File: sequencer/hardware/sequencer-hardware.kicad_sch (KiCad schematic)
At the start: 47 parts, among them J1 Barrel Jack, J2 40Pin 0.1", J3 USB_B_Micro, J4 Conn_01x02_Male, J5 Conn_01x04, J6 TS Out, SW1 PWR, SW2 SW_Push, U1 L7805_A, U2 L7805_D, U3 ICL7660, U4 NCP1117-3.3_TO252, U5 Opamp_Dual

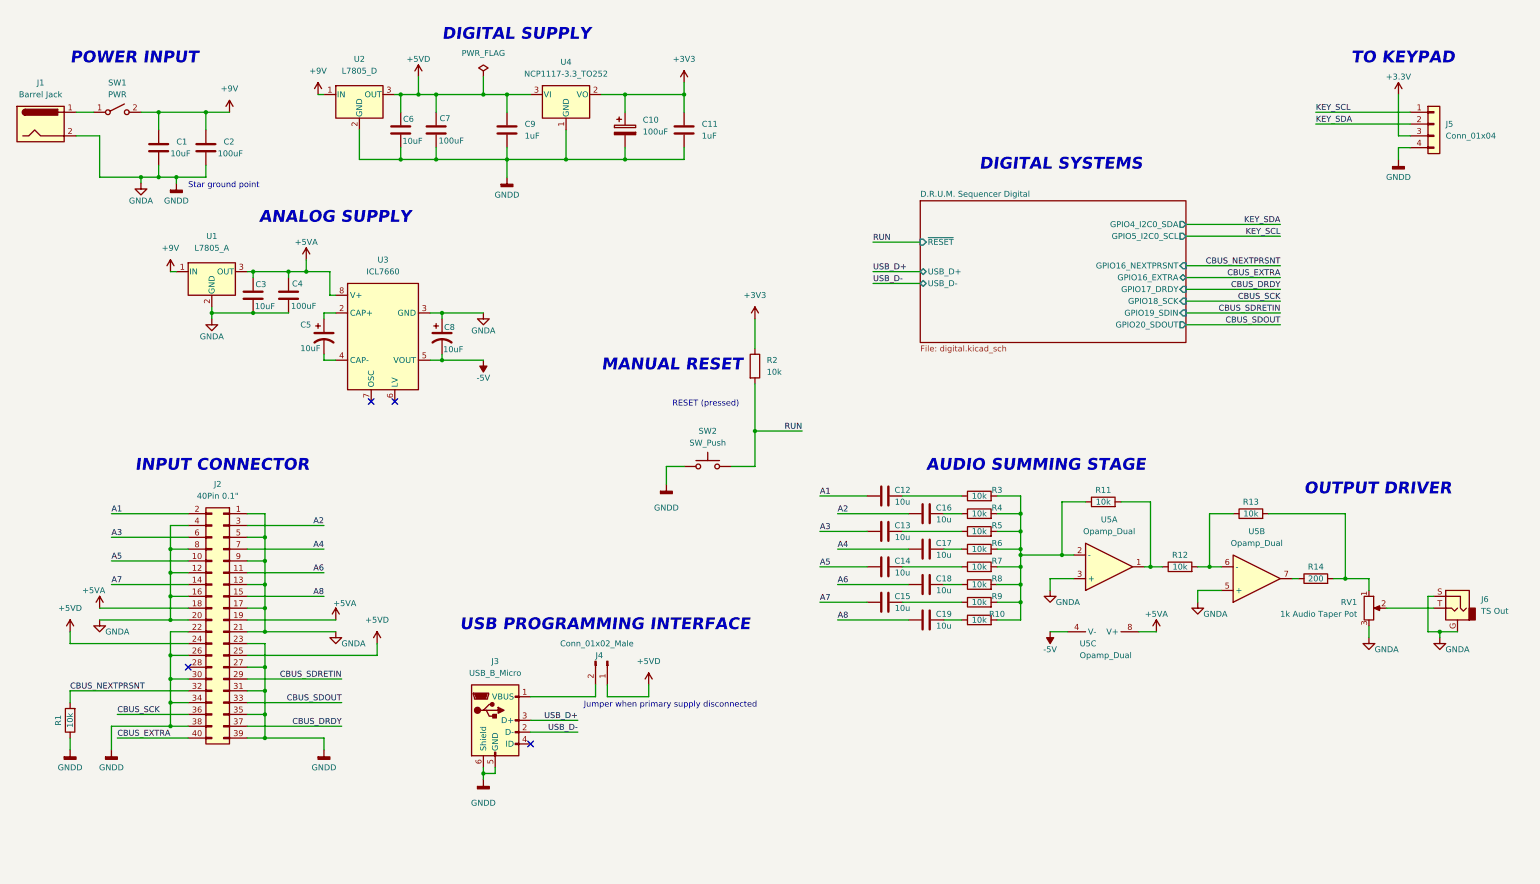
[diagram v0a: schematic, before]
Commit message: Disconnect GNDD from GNDA to prevent routing confusion
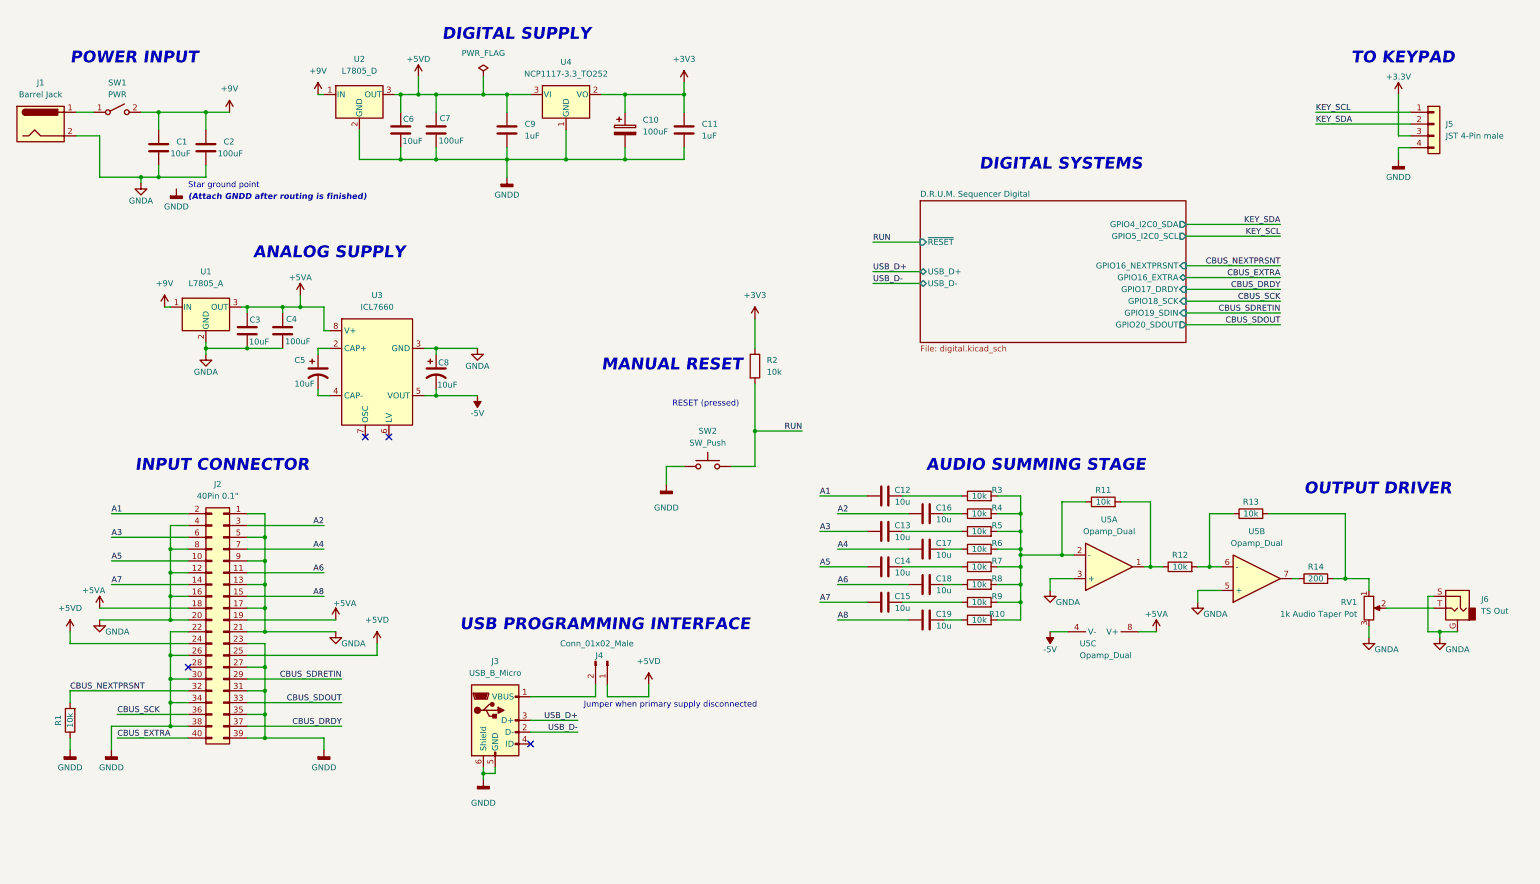
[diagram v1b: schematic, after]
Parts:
- J5: value Conn_01x04 -> JST 4-Pin male; footprint (none) -> Connector_JST:JST_PH_B4B-PH-K_1x04_P2.00mm_Vertical
- R1, R10, R11, R12, R13, R3, R4, R5, R6, R7, R8, R9: footprint (none) -> Resistor_SMD:R_0603_1608Metric_Pad0.98x0.95mm_HandSolder
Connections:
- net GNDA: no longer C10.2, C11.2, C6.2, C7.2, C9.2, J2.22 (Pin_22), J2.23 (Pin_23), J2.26 (Pin_26), J2.27 (Pin_27), J2.30 (Pin_30), J2.31 (Pin_31), J2.34 (Pin_34), J2.35 (Pin_35), J2.38 (Pin_38), J2.39 (Pin_39), J3.5 (GND), J3.6 (Shield), J5.4 (Pin_4), R1.1, SW2.1, U2.2 (GND), U4.1 (GND)
- new net GNDD: C10.2, C11.2, C6.2, C7.2, C9.2, J2.22 (Pin_22), J2.23 (Pin_23), J2.26 (Pin_26), J2.27 (Pin_27), J2.30 (Pin_30), J2.31 (Pin_31), J2.34 (Pin_34), J2.35 (Pin_35), J2.38 (Pin_38), J2.39 (Pin_39), J3.5 (GND), J3.6 (Shield), J5.4 (Pin_4), R1.1, SW2.1, U2.2 (GND), U4.1 (GND)
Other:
- note added: "(Attach GNDD after routing is finished)"
- moved on the sheet: C3, C4, C5, C8, U1, U3

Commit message: Do a lot of random stuff
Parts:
- removed U5: Opamp_Dual, symbol Device:Opamp_Dual
- added U5, U6: OPA703UA, Package_SO:SOIC-8_3.9x4.9mm_P1.27mm, symbol pspice:OPAMP
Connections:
- net +5VA: now also U5.4 (V-), U6.4 (V-)
- net -5V: now also U5.7 (V+), U6.7 (V+)
- net GNDA: now also U5.3 (+), U6.3 (+)
- net at R14.1: now also U6.6
- net at R10.2, R11.1, R3.2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: now also U5.2 (-)
- net at R11.2, R12.1: now also U5.6
- net at R12.2, R13.1: now also U6.2 (-)

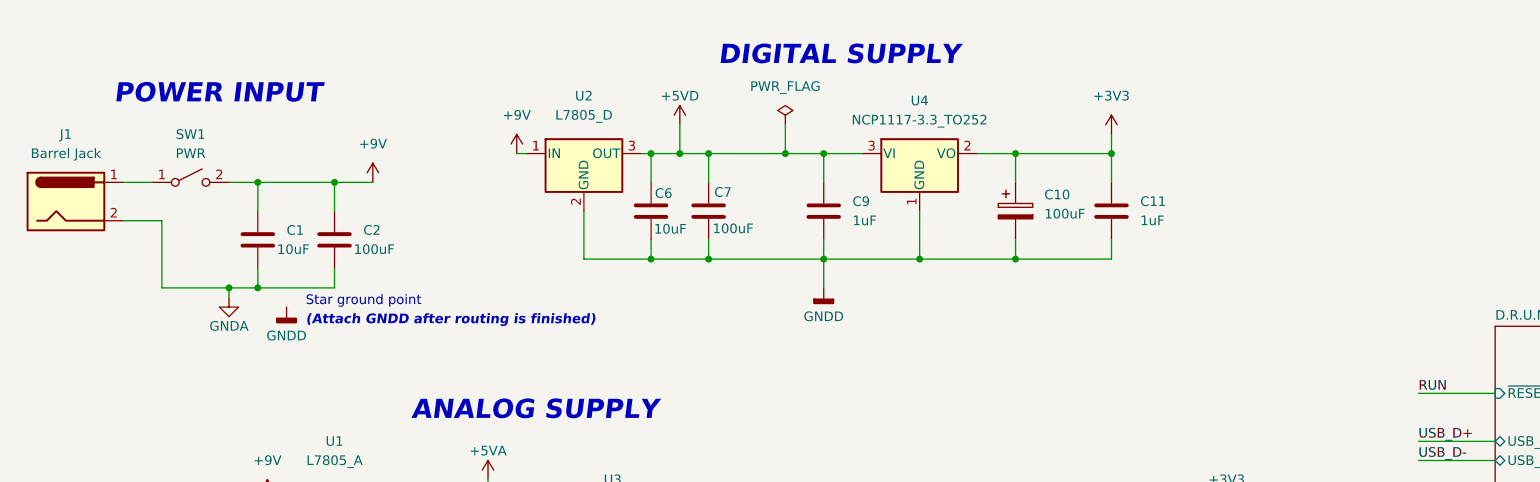
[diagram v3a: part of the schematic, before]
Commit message: Add common mode choke
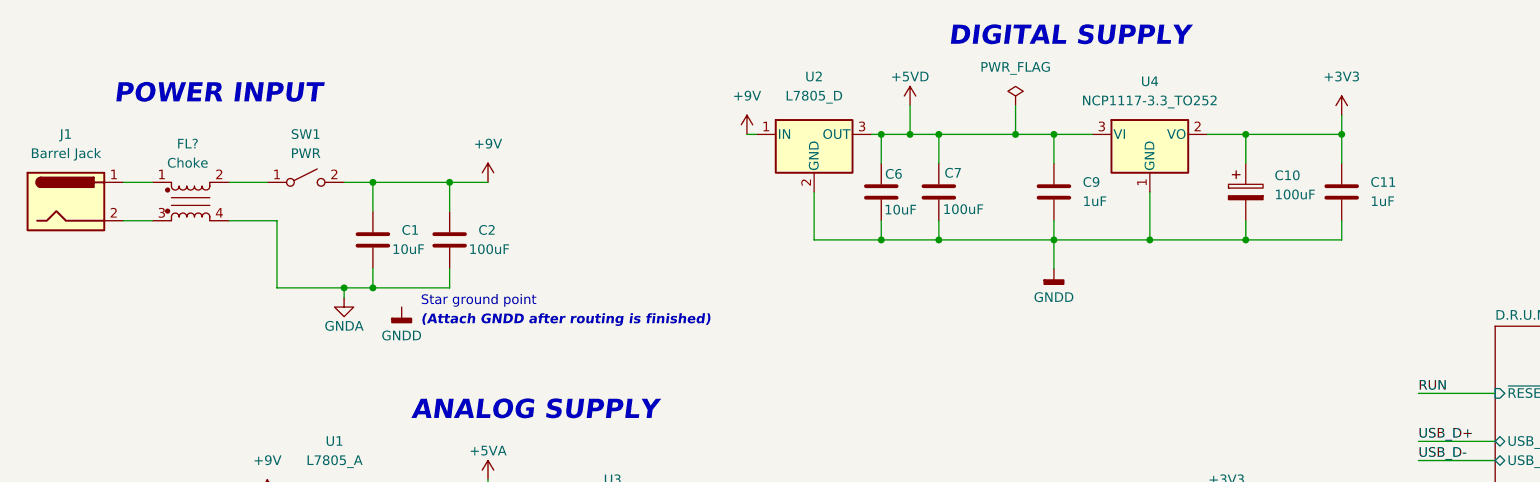
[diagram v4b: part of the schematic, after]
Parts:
- added FL?: Choke, Inductor_THT:Choke_Schaffner_RN102-04-14.0x14.0mm, symbol Filter:Choke_Schaffner_RN102-2-02-1M1
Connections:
- net GNDA: now also FL?.4; no longer J1.2
- net at SW1.1 (A): now also FL?.2; no longer J1.1
- new net: FL?.1, J1.1
- new net: FL?.3, J1.2
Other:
- moved on the sheet: C1, C10, C11, C2, C6, C7, C9, SW1, U2, U4

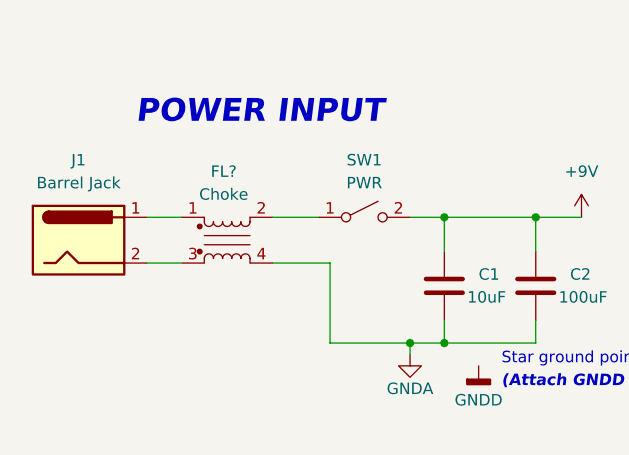
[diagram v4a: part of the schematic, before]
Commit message: Update sequencer-hardware.kicad_sch
footprints updated
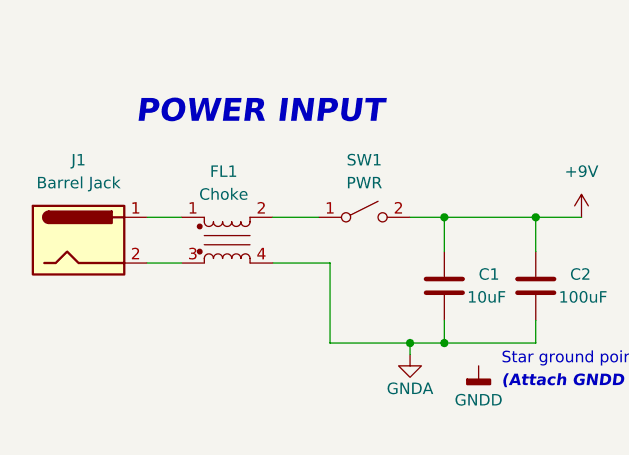
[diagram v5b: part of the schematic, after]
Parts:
- C1, C3, C5, C6, C8: footprint (none) -> Capacitor_SMD:C_1206_3216Metric_Pad1.33x1.80mm_HandSolder
- C2, C4, C7: footprint (none) -> Capacitor_THT:CP_Radial_D8.0mm_P3.50mm
- J1: footprint (none) -> Connector_BarrelJack:BarrelJack_Horizontal
- R14: footprint (none) -> Resistor_SMD:R_0603_1608Metric_Pad0.98x0.95mm_HandSolder
- gave numbers to parts that had none: 1
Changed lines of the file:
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@@
     (property "Reference" "R14" (id 0) (at 294.64 135.89 90))
     (property "Value" "200" (id 1) (at 294.64 138.43 90))
-    (property "Footprint" "" (id 2) (at 294.64 140.208 90)
+    (property "Footprint" "Resistor_SMD:R_0603_1608Metric_Pad0.98x0.95mm_HandSolder" (id 2) (at 294.64 140.208 90)
       (effects (font (size 1.27 1.27)) hide)
     )
@@
       (effects (font (size 1.27 1.27)) (justify left))
     )
-    (property "Footprint" "" (id 2) (at 136.8552 43.18 0)
+    (property "Footprint" "Capacitor_THT:CP_Radial_D8.0mm_P3.50mm" (id 2) (at 136.8552 43.18 0)
       (effects (font (size 1.27 1.27)) hide)
     )
@@
       (effects (font (size 1.27 1.27)) (justify left))
     )
-    (property "Footprint" "" (id 2) (at 80.01 93.98 0)
+    (property "Footprint" "Capacitor_SMD:C_1206_3216Metric_Pad1.33x1.80mm_HandSolder" (id 2) (at 80.01 93.98 0)
       (effects (font (size 1.27 1.27)) hide)
     )
@@
   (symbol (lib_id "Filter:Choke_Schaffner_RN102-2-02-1M1") (at 36.83 40.64 0) (unit 1)
     (in_bom yes) (on_board yes) (fields_autoplaced)
-    (property "Reference" "FL?" (id 0) (at 36.449 33.02 0))
+    (property "Reference" "FL1" (id 0) (at 36.449 33.02 0))
     (property "Value" "Choke" (id 1) (at 36.449 35.56 0))
     (property "Footprint" "Inductor_THT:Choke_Schaffner_RN102-04-14.0x14.0mm" (id 2) (at 36.83 40.64 0)
@@
       (effects (font (size 1.27 1.27)) (justify left))
     )
-    (property "Footprint" "" (id 2) (at 105.41 93.98 0)
+    (property "Footprint" "Capacitor_SMD:C_1206_3216Metric_Pad1.33x1.80mm_HandSolder" (id 2) (at 105.41 93.98 0)
       (effects (font (size 1.27 1.27)) hide)
     )
@@
       (effects (font (size 1.27 1.27)) (justify left))
     )
-    (property "Footprint" "" (id 2) (at 72.0852 49.53 0)
+    (property "Footprint" "Capacitor_THT:CP_Radial_D8.0mm_P3.50mm" (id 2) (at 72.0852 49.53 0)
       (effects (font (size 1.27 1.27)) hide)
     )
@@
       (effects (font (size 1.27 1.27)) (justify left))
     )
-    (property "Footprint" "" (id 2) (at 73.3552 88.9 0)
+    (property "Footprint" "Capacitor_THT:CP_Radial_D8.0mm_P3.50mm" (id 2) (at 73.3552 88.9 0)
       (effects (font (size 1.27 1.27)) hide)
     )
@@
       (effects (font (size 1.27 1.27)) (justify left))
     )
-    (property "Footprint" "" (id 2) (at 61.9252 49.53 0)
+    (property "Footprint" "Capacitor_SMD:C_1206_3216Metric_Pad1.33x1.80mm_HandSolder" (id 2) (at 61.9252 49.53 0)
       (effects (font (size 1.27 1.27)) hide)
     )
@@
       (effects (font (size 1.27 1.27)) (justify left))
     )
-    (property "Footprint" "" (id 2) (at 129.2352 43.18 0)
+    (property "Footprint" "Capacitor_SMD:C_1206_3216Metric_Pad1.33x1.80mm_HandSolder" (id 2) (at 129.2352 43.18 0)
       (effects (font (size 1.27 1.27)) hide)
     )
@@
       (effects (font (size 1.27 1.27)) (justify left))
     )
-    (property "Footprint" "" (id 2) (at 65.7352 88.9 0)
+    (property "Footprint" "Capacitor_SMD:C_1206_3216Metric_Pad1.33x1.80mm_HandSolder" (id 2) (at 65.7352 88.9 0)
       (effects (font (size 1.27 1.27)) hide)
     )
@@
     (property "Reference" "J1" (id 0) (at 20.32 31.75 0))
     (property "Value" "Barrel Jack" (id 1) (at 20.32 34.29 0))
-    (property "Footprint" "" (id 2) (at 21.59 41.656 0)
+    (property "Footprint" "Connector_BarrelJack:BarrelJack_Horizontal" (id 2) (at 21.59 41.656 0)
       (effects (font (size 1.27 1.27)) hide)
     )
@@
     )
     (path "/a16cb1a3-db57-4f1c-bb1b-9a970683e6ab"
-      (reference "C1") (unit 1) (value "10uF") (footprint "")
+      (reference "C1") (unit 1) (value "10uF") (footprint "Capacitor_SMD:C_1206_3216Metric_Pad1.33x1.80mm_HandSolder")
     )
     (path "/71bcca76-dcd0-45b6-a387-efe1c2713601"
-      (reference "C2") (unit 1) (value "100uF") (footprint "")
+      (reference "C2") (unit 1) (value "100uF") (footprint "Capacitor_THT:CP_Radial_D8.0mm_P3.50mm")
     )
     (path "/e263c6c9-245b-49e7-9320-f31d739535dc"
-      (reference "C3") (unit 1) (value "10uF") (footprint "")
+      (reference "C3") (unit 1) (value "10uF") (footprint "Capacitor_SMD:C_1206_3216Metric_Pad1.33x1.80mm_HandSolder")
     )
     (path "/71e0d646-a0ed-4fb3-a03c-8b2c3fdd09f7"
-      (reference "C4") (unit 1) (value "100uF") (footprint "")
+      (reference "C4") (unit 1) (value "100uF") (footprint "Capacitor_THT:CP_Radial_D8.0mm_P3.50mm")
     )
     (path "/2dada4ad-74b7-48ca-bf7d-949ba934d9e5"
-      (reference "C5") (unit 1) (value "10uF") (footprint "")
+      (reference "C5") (unit 1) (value "10uF") (footprint "Capacitor_SMD:C_1206_3216Metric_Pad1.33x1.80mm_HandSolder")
     )
     (path "/cd2a5532-6b56-492a-8903-636dc296dbd0"
-      (reference "C6") (unit 1) (value "10uF") (footprint "")
+      (reference "C6") (unit 1) (value "10uF") (footprint "Capacitor_SMD:C_1206_3216Metric_Pad1.33x1.80mm_HandSolder")
     )
     (path "/282fd59f-94a4-4f57-984e-73fc48394377"
-      (reference "C7") (unit 1) (value "100uF") (footprint "")
+      (reference "C7") (unit 1) (value "100uF") (footprint "Capacitor_THT:CP_Radial_D8.0mm_P3.50mm")
     )
     (path "/6e81a48f-85a2-4208-99b3-eebb27823884"
-      (reference "C8") (unit 1) (value "10uF") (footprint "")
+      (reference "C8") (unit 1) (value "10uF") (footprint "Capacitor_SMD:C_1206_3216Metric_Pad1.33x1.80mm_HandSolder")
     )
     (path "/d6a8a65c-0f5c-4d9a-bc07-043c4b864dc1"
@@
     )
     (path "/6b701ad3-5280-44c7-bba3-d6e8f0b30748"
-      (reference "FL?") (unit 1) (value "Choke") (footprint "Inductor_THT:Choke_Schaffner_RN102-04-14.0x14.0mm")
+      (reference "FL1") (unit 1) (value "Choke") (footprint "Inductor_THT:Choke_Schaffner_RN102-04-14.0x14.0mm")
     )
     (path "/e7d77e35-7d0f-418c-bddb-e70c65e01157"
-      (reference "J1") (unit 1) (value "Barrel Jack") (footprint "")
+      (reference "J1") (unit 1) (value "Barrel Jack") (footprint "Connector_BarrelJack:BarrelJack_Horizontal")
     )
     (path "/e93c3d17-0d0d-4ac2-84d5-add74a1e2359"
@@
     )
     (path "/0278d084-f4e5-490f-8d53-0d1571fdb41b"
-      (reference "R14") (unit 1) (value "200") (footprint "")
+      (reference "R14") (unit 1) (value "200") (footprint "Resistor_SMD:R_0603_1608Metric_Pad0.98x0.95mm_HandSolder")
     )
     (path "/56dcffd5-e973-4f89-956d-68b94266f270/fc05d683-1899-4673-bcc5-271a1835594a"

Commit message: more footprints
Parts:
- J6: footprint (none) -> Connector_Audio:Jack_6.35mm_Neutrik_NRJ6HF-AU_Horizontal
- RV1: footprint (none) -> custom:LINPOT-10KDB
- U1, U2: footprint (none) -> Package_TO_SOT_THT:TO-220-3_Horizontal_TabDown
- U3: footprint (none) -> Package_SO:SOIC-8_3.9x4.9mm_P1.27mm
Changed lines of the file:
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@@
       (effects (font (size 1.27 1.27)) (justify right))
     )
-    (property "Footprint" "" (id 2) (at 306.07 144.78 0)
+    (property "Footprint" "custom:LINPOT-10KDB" (id 2) (at 306.07 144.78 0)
       (effects (font (size 1.27 1.27)) hide)
     )
@@
     (property "Reference" "U1" (id 0) (at 55.88 72.39 0))
     (property "Value" "L7805_A" (id 1) (at 55.88 74.93 0))
-    (property "Footprint" "" (id 2) (at 56.515 83.82 0)
+    (property "Footprint" "Package_TO_SOT_THT:TO-220-3_Horizontal_TabDown" (id 2) (at 56.515 83.82 0)
       (effects (font (size 1.27 1.27) italic) (justify left) hide)
     )
@@
     (property "Reference" "U3" (id 0) (at 92.71 77.47 0))
     (property "Value" "ICL7660" (id 1) (at 92.71 80.01 0))
-    (property "Footprint" "" (id 2) (at 95.25 95.25 0)
+    (property "Footprint" "Package_SO:SOIC-8_3.9x4.9mm_P1.27mm" (id 2) (at 95.25 95.25 0)
       (effects (font (size 1.27 1.27)) hide)
     )
@@
       (effects (font (size 1.27 1.27)) (justify right))
     )
-    (property "Footprint" "" (id 2) (at 325.12 144.78 0)
+    (property "Footprint" "Connector_Audio:Jack_6.35mm_Neutrik_NRJ6HF-AU_Horizontal" (id 2) (at 325.12 144.78 0)
       (effects (font (size 1.27 1.27)) hide)
     )
@@
     (property "Reference" "U2" (id 0) (at 119.38 24.13 0))
     (property "Value" "L7805_D" (id 1) (at 119.38 26.67 0))
-    (property "Footprint" "" (id 2) (at 120.015 35.56 0)
+    (property "Footprint" "Package_TO_SOT_THT:TO-220-3_Horizontal_TabDown" (id 2) (at 120.015 35.56 0)
       (effects (font (size 1.27 1.27) italic) (justify left) hide)
     )
@@
     )
     (path "/9aace521-c29e-4538-a0ed-3cdf64db2fd6"
-      (reference "J6") (unit 1) (value "TS Out") (footprint "")
+      (reference "J6") (unit 1) (value "TS Out") (footprint "Connector_Audio:Jack_6.35mm_Neutrik_NRJ6HF-AU_Horizontal")
     )
     (path "/56dcffd5-e973-4f89-956d-68b94266f270/4e8db76f-d9b3-4673-8ae0-baf543e2e32d"
@@
     )
     (path "/2cc3a222-efe9-400d-8ec9-be9ab26a505c"
-      (reference "RV1") (unit 1) (value "1k Audio Taper Pot") (footprint "")
+      (reference "RV1") (unit 1) (value "1k Audio Taper Pot") (footprint "custom:LINPOT-10KDB")
     )
     (path "/622d6f91-69b3-4cb6-8ec6-4ea59f7b3e15"
@@
     )
     (path "/359d6b0b-5f28-4c5f-9c0e-eb52ae372b11"
-      (reference "U1") (unit 1) (value "L7805_A") (footprint "")
+      (reference "U1") (unit 1) (value "L7805_A") (footprint "Package_TO_SOT_THT:TO-220-3_Horizontal_TabDown")
     )
     (path "/ca9611d6-76b3-4219-bb41-c1da253c11b4"
-      (reference "U2") (unit 1) (value "L7805_D") (footprint "")
+      (reference "U2") (unit 1) (value "L7805_D") (footprint "Package_TO_SOT_THT:TO-220-3_Horizontal_TabDown")
     )
     (path "/67731542-430c-42f7-87ed-59c57eb6fef9"
-      (reference "U3") (unit 1) (value "ICL7660") (footprint "")
+      (reference "U3") (unit 1) (value "ICL7660") (footprint "Package_SO:SOIC-8_3.9x4.9mm_P1.27mm")
     )
     (path "/e30197c3-13c5-4b66-bff7-7f72d9b4695c"

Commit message: Adjust component placement
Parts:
- SW1: footprint (none) -> Connector_PinHeader_2.00mm:PinHeader_1x02_P2.00mm_Vertical
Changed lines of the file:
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@@
     (property "Reference" "SW1" (id 0) (at 52.07 31.75 0))
     (property "Value" "PWR" (id 1) (at 52.07 34.29 0))
-    (property "Footprint" "" (id 2) (at 52.07 38.1 0)
+    (property "Footprint" "Connector_PinHeader_2.00mm:PinHeader_1x02_P2.00mm_Vertical" (id 2) (at 52.07 38.1 0)
       (effects (font (size 1.27 1.27)) hide)
     )
@@
     )
     (path "/622d6f91-69b3-4cb6-8ec6-4ea59f7b3e15"
-      (reference "SW1") (unit 1) (value "PWR") (footprint "")
+      (reference "SW1") (unit 1) (value "PWR") (footprint "Connector_PinHeader_2.00mm:PinHeader_1x02_P2.00mm_Vertical")
     )
     (path "/cfd12834-aaf9-4680-8c75-780e13783c78"
